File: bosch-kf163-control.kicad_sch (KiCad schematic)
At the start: 35 parts, among them J101 TGA, J102 PROG, Q101 DTC143ZE, Q102 DTC143ZE, Q103 DTC143ZE, Q104 DTC143ZE, U101 74HC165D, U102 AMS1117-3.3, U103 ESP32-WROOM-32U

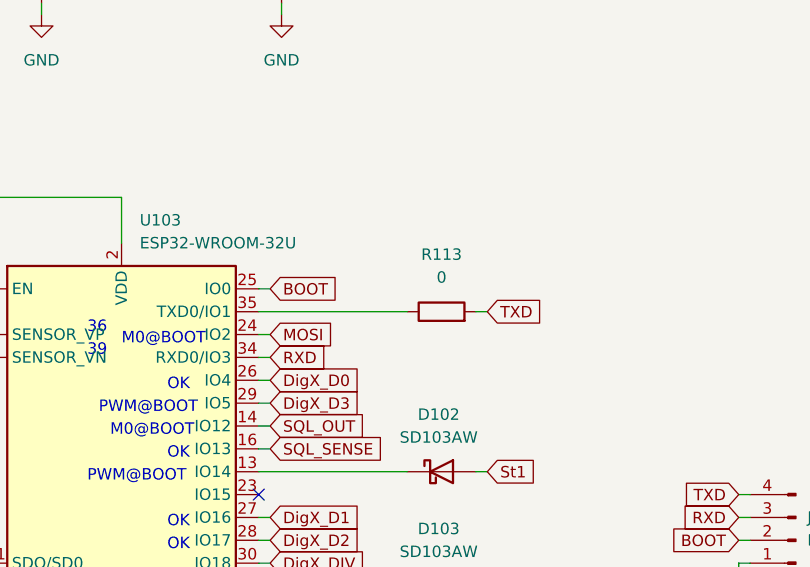
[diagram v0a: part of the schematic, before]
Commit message: sheet comments, schematic variants, removed txd resistor
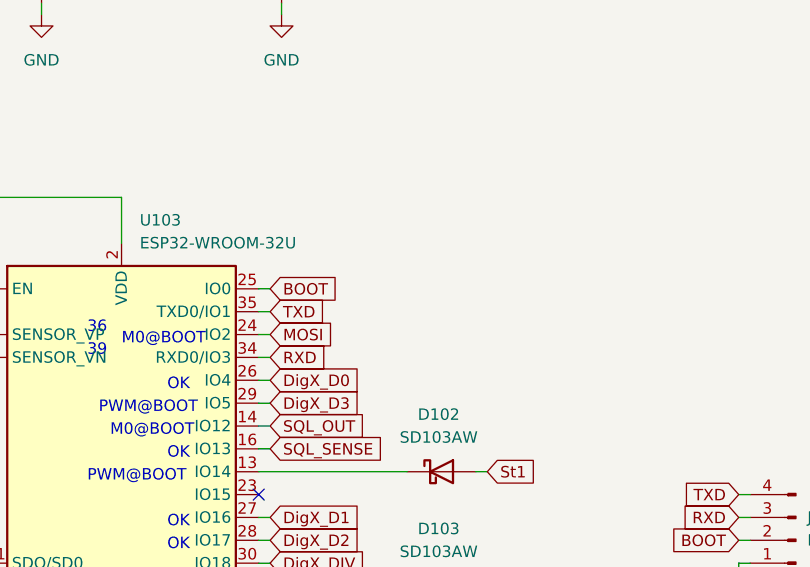
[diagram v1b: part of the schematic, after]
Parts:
- removed R113: 0, Resistor_SMD:R_0603_1608Metric, symbol Device:R
- C101, D102, D103, Q104, R101, R102, R103, R104, R105, R106, R107, R108, R109, R110, U101: variant (none) -> ControlHead
- C102, C103, C104, C105, C106, D101, J101, J102, Q101, Q102, Q103, R111, R112, R114, U102, U103: variant (none) -> Base
- R115, R116, R117: variant (none) -> ExternalUART
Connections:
- net TXD: now also U103.35 (TXD0/IO1)
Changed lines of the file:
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@@
-    (stroke (width 0) (type default) (color 0 0 0 0))
-  )
-  (wire (pts (xy 128.27 123.19) (xy 111.76 123.19))
     (stroke (width 0) (type default) (color 0 0 0 0))
   )
@@
     (stroke (width 0) (type default) (color 0 0 0 0))
   )
+  (wire (pts (xy 113.03 123.19) (xy 111.76 123.19))
+    (stroke (width 0) (type default) (color 0 0 0 0))
+  )
   (wire (pts (xy 171.45 58.42) (xy 232.41 58.42))
     (stroke (width 0) (type default) (color 0 0 0 0))
@@
   )
   (wire (pts (xy 166.37 68.58) (xy 165.1 68.58))
-    (stroke (width 0) (type default) (color 0 0 0 0))
-  )
-  (wire (pts (xy 137.16 123.19) (xy 135.89 123.19))
     (stroke (width 0) (type default) (color 0 0 0 0))
   )
@@
     )
   )
-  (global_label "TXD" (shape input) (at 137.16 123.19 0) (fields_autoplaced)
-    (effects (font (size 1.27 1.27)) (justify left))
-    (property "Intersheet References" "${INTERSHEET_REFS}" (id 0) (at 143.0202 123.1106 0)
+  (global_label "TXD" (shape input) (at 113.03 123.19 0) (fields_autoplaced)
+    (effects (font (size 1.27 1.27)) (justify left))
+    (property "Intersheet References" "${INTERSHEET_REFS}" (id 0) (at 118.8902 123.1106 0)
       (effects (font (size 1.27 1.27)) (justify left) hide)
     )
@@
       (effects (font (size 1.27 1.27)) hide)
     )
+    (property "variant" "ControlHead" (id 5) (at 132.08 140.97 0)
+      (effects (font (size 1.27 1.27)) hide)
+    )
     (pin "1")
     (pin "2")
@@
     )
     (property "LCSC" "C14663" (id 4) (at 55.88 115.57 0)
+      (effects (font (size 1.27 1.27)) hide)
+    )
+    (property "variant" "Base" (id 5) (at 55.88 115.57 0)
       (effects (font (size 1.27 1.27)) hide)
     )
@@
       (effects (font (size 1.27 1.27)) hide)
     )
+    (property "variant" "ControlHead" (id 5) (at 171.45 27.94 0)
+      (effects (font (size 1.27 1.27)) hide)
+    )
     (pin "1")
     (pin "2")
@@
     )
     (property "LCSC" "C5613" (id 4) (at 245.11 55.88 0)
+      (effects (font (size 1.27 1.27)) hide)
+    )
+    (property "variant" "ControlHead" (id 5) (at 245.11 55.88 0)
       (effects (font (size 1.27 1.27)) hide)
     )
@@
       (effects (font (size 1.27 1.27)) hide)
     )
+    (property "variant" "ControlHead" (id 5) (at 201.93 27.94 0)
+      (effects (font (size 1.27 1.27)) hide)
+    )
     (pin "1")
     (pin "2")
@@
       (effects (font (size 1.27 1.27)) hide)
     )
+    (property "variant" "ControlHead" (id 5) (at 154.94 27.94 0)
+      (effects (font (size 1.27 1.27)) hide)
+    )
     (pin "1")
     (pin "2")
@@
       (effects (font (size 1.27 1.27)) hide)
     )
+    (property "variant" "ControlHead" (id 5) (at 179.07 27.94 0)
+      (effects (font (size 1.27 1.27)) hide)
+    )
     (pin "1")
     (pin "2")
@@
     )
     (property "LCSC" "C14663" (id 4) (at 67.31 134.62 0)
+      (effects (font (size 1.27 1.27)) hide)
+    )
+    (property "variant" "Base" (id 5) (at 67.31 134.62 0)
       (effects (font (size 1.27 1.27)) hide)
     )
@@
       (effects (font (size 1.27 1.27)) hide)
     )
+    (property "variant" "ExternalUART" (id 5) (at 161.29 71.12 90)
+      (effects (font (size 1.27 1.27)) hide)
+    )
     (pin "1")
     (pin "2")
@@
       (effects (font (size 1.27 1.27)) hide)
     )
+    (property "variant" "Base" (id 5) (at 63.5 83.82 0)
+      (effects (font (size 1.27 1.27)) hide)
+    )
     (pin "1")
     (pin "2")
@@
       (effects (font (size 1.27 1.27)) hide)
     )
+    (property "variant" "ControlHead" (id 5) (at 204.47 83.82 0)
+      (effects (font (size 1.27 1.27)) hide)
+    )
     (pin "1")
     (pin "2")
     (pin "3")
-  )
-  (symbol (lib_id "Device:R") (at 132.08 123.19 90) (unit 1)
-    (in_bom yes) (on_board yes) (fields_autoplaced)
-    (property "Reference" "R113" (id 0) (at 132.08 116.84 90))
-    (property "Value" "0" (id 1) (at 132.08 119.38 90))
-    (property "Footprint" "Resistor_SMD:R_0603_1608Metric" (id 2) (at 132.08 124.968 90)
-      (effects (font (size 1.27 1.27)) hide)
-    )
-    (property "Datasheet" "~" (id 3) (at 132.08 123.19 0)
-      (effects (font (size 1.27 1.27)) hide)
-    )
-    (property "LCSC" "C100044" (id 4) (at 132.08 123.19 0)
-      (effects (font (size 1.27 1.27)) hide)
-    )
-    (pin "1")
-    (pin "2")
   )
   (symbol (lib_id "Device:R") (at 209.55 27.94 0) (unit 1)
@@
       (effects (font (size 1.27 1.27)) hide)
     )
+    (property "variant" "ControlHead" (id 5) (at 209.55 27.94 0)
+      (effects (font (size 1.27 1.27)) hide)
+    )
     (pin "1")
     (pin "2")
@@
     )
     (property "Datasheet" "~" (id 3) (at 171.45 148.59 0)
+      (effects (font (size 1.27 1.27)) hide)
+    )
+    (property "variant" "Base" (id 4) (at 171.45 148.59 0)
       (effects (font (size 1.27 1.27)) hide)
     )
@@
       (effects (font (size 1.27 1.27)) hide)
     )
+    (property "variant" "Base" (id 5) (at 113.03 83.82 0)
+      (effects (font (size 1.27 1.27)) hide)
+    )
     (pin "1")
     (pin "2")
@@
       (effects (font (size 1.27 1.27)) hide)
     )
+    (property "variant" "ControlHead" (id 5) (at 163.83 27.94 0)
+      (effects (font (size 1.27 1.27)) hide)
+    )
     (pin "1")
     (pin "2")
@@
       (effects (font (size 1.27 1.27)) hide)
     )
+    (property "variant" "Base" (id 5) (at 59.69 53.34 0)
+      (effects (font (size 1.27 1.27)) hide)
+    )
     (pin "1")
     (pin "2")
@@
       (effects (font (size 1.27 1.27)) hide)
     )
+    (property "variant" "ControlHead" (id 5) (at 147.32 27.94 0)
+      (effects (font (size 1.27 1.27)) hide)
+    )
     (pin "1")
     (pin "2")
@@
     )
     (property "LCSC" "C105428" (id 4) (at 194.31 27.94 0)
+      (effects (font (size 1.27 1.27)) hide)
+    )
+    (property "variant" "ControlHead" (id 5) (at 194.31 27.94 0)
       (effects (font (size 1.27 1.27)) hide)
     )
@@
       (effects (font (size 1.27 1.27)) hide)
     )
+    (property "variant" "ExternalUART" (id 5) (at 161.29 68.58 90)
+      (effects (font (size 1.27 1.27)) hide)
+    )
     (pin "1")
     (pin "2")
@@
     )
     (property "LCSC" "C2922482" (id 4) (at 44.45 115.57 0)
+      (effects (font (size 1.27 1.27)) hide)
+    )
+    (property "variant" "Base" (id 5) (at 44.45 115.57 0)
       (effects (font (size 1.27 1.27)) hide)
     )
@@
       (effects (font (size 1.27 1.27)) hide)
     )
+    (property "variant" "ControlHead" (id 5) (at 240.03 31.75 0)
+      (effects (font (size 1.27 1.27)) hide)
+    )
     (pin "1")
     (pin "2")
@@
     )
     (property "LCSC" "C181204" (id 4) (at 132.08 153.67 0)
+      (effects (font (size 1.27 1.27)) hide)
+    )
+    (property "variant" "ControlHead" (id 5) (at 132.08 153.67 0)
       (effects (font (size 1.27 1.27)) hide)
     )
@@
       (effects (font (size 1.27 1.27)) hide)
     )
+    (property "variant" "ExternalUART" (id 5) (at 161.29 73.66 90)
+      (effects (font (size 1.27 1.27)) hide)
+    )
     (pin "1")
     (pin "2")
@@
       (effects (font (size 1.27 1.27)) hide)
     )
+    (property "variant" "ControlHead" (id 5) (at 217.17 27.94 0)
+      (effects (font (size 1.27 1.27)) hide)
+    )
     (pin "1")
     (pin "2")
@@
       (effects (font (size 1.27 1.27)) hide)
     )
+    (property "variant" "Base" (id 5) (at 67.31 115.57 0)
+      (effects (font (size 1.27 1.27)) hide)
+    )
     (pin "1")
     (pin "2")
@@
     )
     (property "LCSC" "C328062" (id 4) (at 96.52 151.13 0)
+      (effects (font (size 1.27 1.27)) hide)
+    )
+    (property "variant" "Base" (id 5) (at 96.52 151.13 0)
       (effects (font (size 1.27 1.27)) hide)
     )
@@
       (effects (font (size 1.27 1.27)) hide)
     )
+    (property "variant" "Base" (id 5) (at 105.41 67.31 0)
+      (effects (font (size 1.27 1.27)) hide)
+    )
     (pin "1")
     (pin "2")
@@
       (effects (font (size 1.27 1.27)) hide)
     )
+    (property "variant" "Base" (id 5) (at 86.36 83.82 0)
+      (effects (font (size 1.27 1.27)) hide)
+    )
     (pin "1")
     (pin "2")
@@
       (effects (font (size 1.27 1.27)) hide)
     )
+    (property "variant" "ControlHead" (id 5) (at 186.69 27.94 0)
+      (effects (font (size 1.27 1.27)) hide)
+    )
     (pin "1")
     (pin "2")
@@
       (effects (font (size 1.27 1.27)) hide)
     )
+    (property "variant" "Base" (id 5) (at 227.33 119.38 0)
+      (effects (font (size 1.27 1.27)) hide)
+    )
     (pin "1")
     (pin "2")
@@
     )
     (property "LCSC" "C105428" (id 4) (at 53.34 46.99 0)
+      (effects (font (size 1.27 1.27)) hide)
+    )
+    (property "variant" "Base" (id 5) (at 53.34 46.99 0)
       (effects (font (size 1.27 1.27)) hide)
     )
@@
       (effects (font (size 1.27 1.27)) hide)
     )
+    (property "variant" "Base" (id 5) (at 215.9 114.3 0)
+      (effects (font (size 1.27 1.27)) hide)
+    )
     (pin "1")
     (pin "2")
@@
     )
     (property "LCSC" "C2922482" (id 4) (at 200.66 119.38 0)
+      (effects (font (size 1.27 1.27)) hide)
+    )
+    (property "variant" "Base" (id 5) (at 200.66 119.38 0)
       (effects (font (size 1.27 1.27)) hide)
     )
@@
     )
     (property "LCSC" "C115248" (id 4) (at 132.08 58.42 0)
+      (effects (font (size 1.27 1.27)) hide)
+    )
+    (property "variant" "Base" (id 5) (at 132.08 58.42 0)
       (effects (font (size 1.27 1.27)) hide)
     )
@@
       (reference "R112") (unit 1) (value "4.7k") (footprint "Resistor_SMD:R_0603_1608Metric")
     )
-    (path "/7abb8a0b-1d5b-4302-94e1-aeade47564fe"
-      (reference "R113") (unit 1) (value "0") (footprint "Resistor_SMD:R_0603_1608Metric")
-    )
     (path "/cad4dc45-bcbd-4b5d-9e70-45d84f741c02"
